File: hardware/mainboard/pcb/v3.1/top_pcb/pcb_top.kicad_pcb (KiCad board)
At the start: 2 copper layers, 105 x 47 mm, 20 parts, among them J1 molex1x03, U1 ATtiny1626, U2 74hc4066, U3 74hc4066, U4 74hc4066, U5 74hc4066, U6 74hc4066, U7 74hc4066, U8 74hc4066, U9 74hc4066

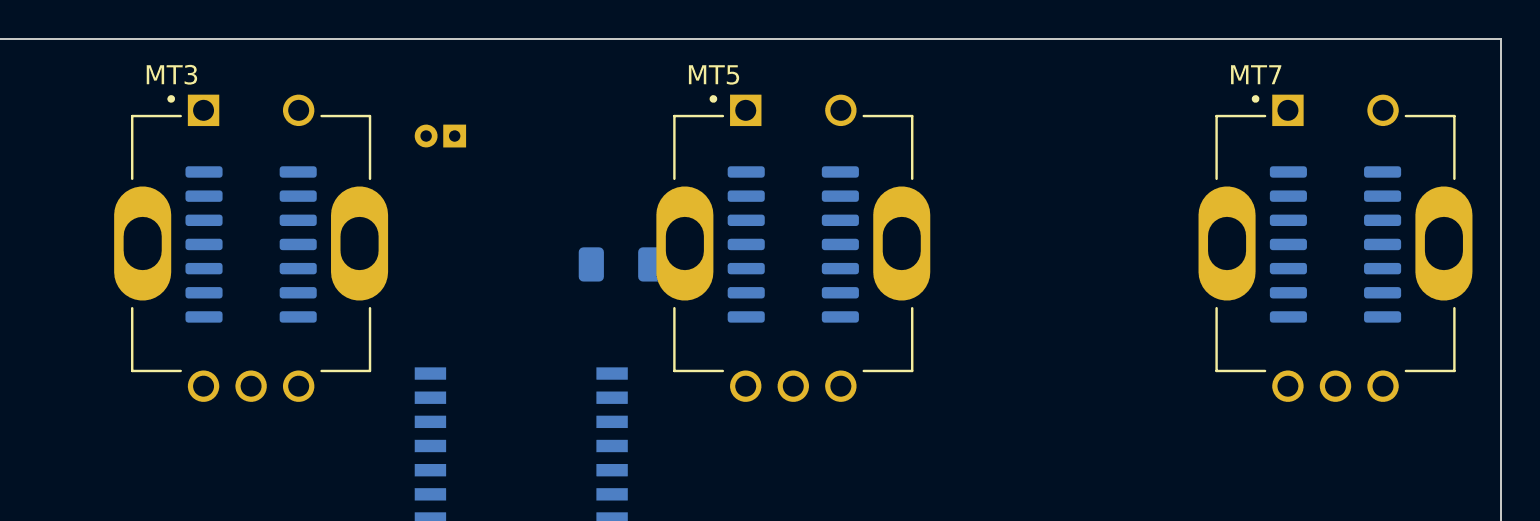
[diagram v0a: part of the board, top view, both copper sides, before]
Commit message: align top encoder
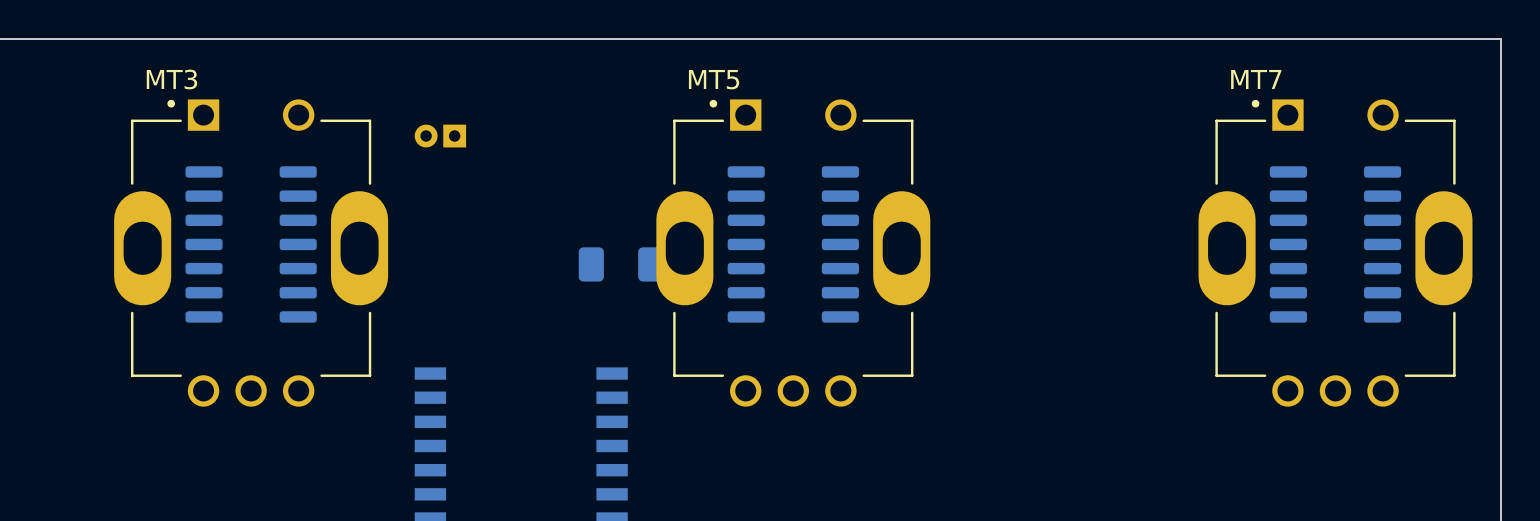
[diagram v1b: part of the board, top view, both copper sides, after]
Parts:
- moved MT3 0.25 mm to (94.3, 49.0)
- moved MT5 0.25 mm to (122.8, 49.0)
- moved MT7 0.25 mm to (151.3, 49.0)
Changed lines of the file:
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@@
   )
   (footprint "3dAudioFoot:XDCR_PEC11R-4215F-S0024" locked (layer "F.Cu")
-    (at 151.3 48.75)
+    (at 151.3 49)
     (property "Check_prices" "https://www.snapeda.com/parts/PEC11R-4215F-S0024/Bourns/view-part/?ref=eda")
     (property "Description" "\nEncoder,Rotary,24 Detents,15 mm, Shaft,Switch | Bourns PEC11R-4215F-S0024\n")
@@
   )
   (footprint "3dAudioFoot:XDCR_PEC11R-4215F-S0024" locked (layer "F.Cu")
-    (at 122.8 48.75)
+    (at 122.8 49)
     (property "Check_prices" "https://www.snapeda.com/parts/PEC11R-4215F-S0024/Bourns/view-part/?ref=eda")
     (property "Description" "\nEncoder,Rotary,24 Detents,15 mm, Shaft,Switch | Bourns PEC11R-4215F-S0024\n")
@@
   )
   (footprint "3dAudioFoot:XDCR_PEC11R-4215F-S0024" locked (layer "F.Cu")
-    (at 94.3 48.75)
-    (property "Check_prices" "https://www.snapeda.com/parts/PEC11R-4215F-S0024/Bourns/view-part/?ref=eda")
-    (property "Description" "\nEncoder,Rotary,24 Detents,15 mm, Shaft,Switch | Bourns PEC11R-4215F-S0024\n")
+    (at 94.3 49)
+    (property "Check_prices" "https://www.snapeda.com/parts/PEC11R-4215F-S0024/Bourns/view-part/?ref=eda")
+    (property "Description" "\nEncoder,Rotary,24 Detents,15 mm, Shaft,Switch | Bourns PEC11R-4215F-S0024\n")
